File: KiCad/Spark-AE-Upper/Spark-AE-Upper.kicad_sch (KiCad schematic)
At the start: 15 parts, among them J1 SSM-120-L-SV-BE, J2 SSM-120-L-SV-BE, J4 Conn_02x05_Odd_Even, J5 Conn_01x08_Socket, J6 Conn_01x08_Socket, J7 UJ32-C-V-G-TH-5-P24-TR, SW1 SW_Push, SW2 SW_Push, U1 PJS008U-3000-0, U2 Daisy_Seed

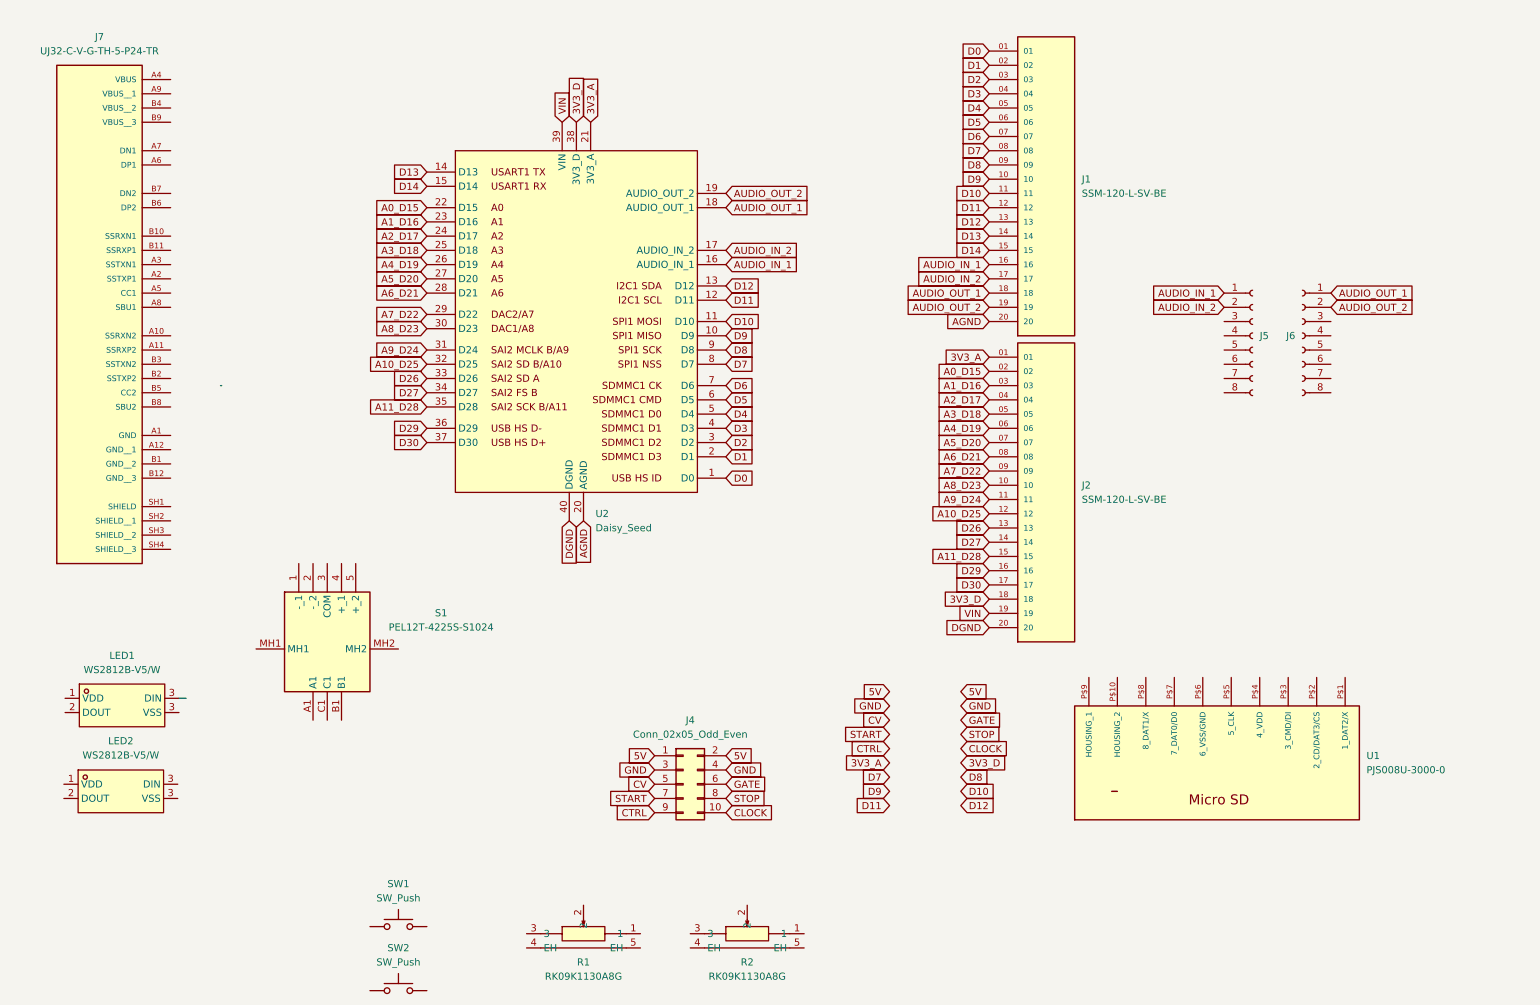
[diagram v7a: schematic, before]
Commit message: renamed nets to match pod and added arc connector
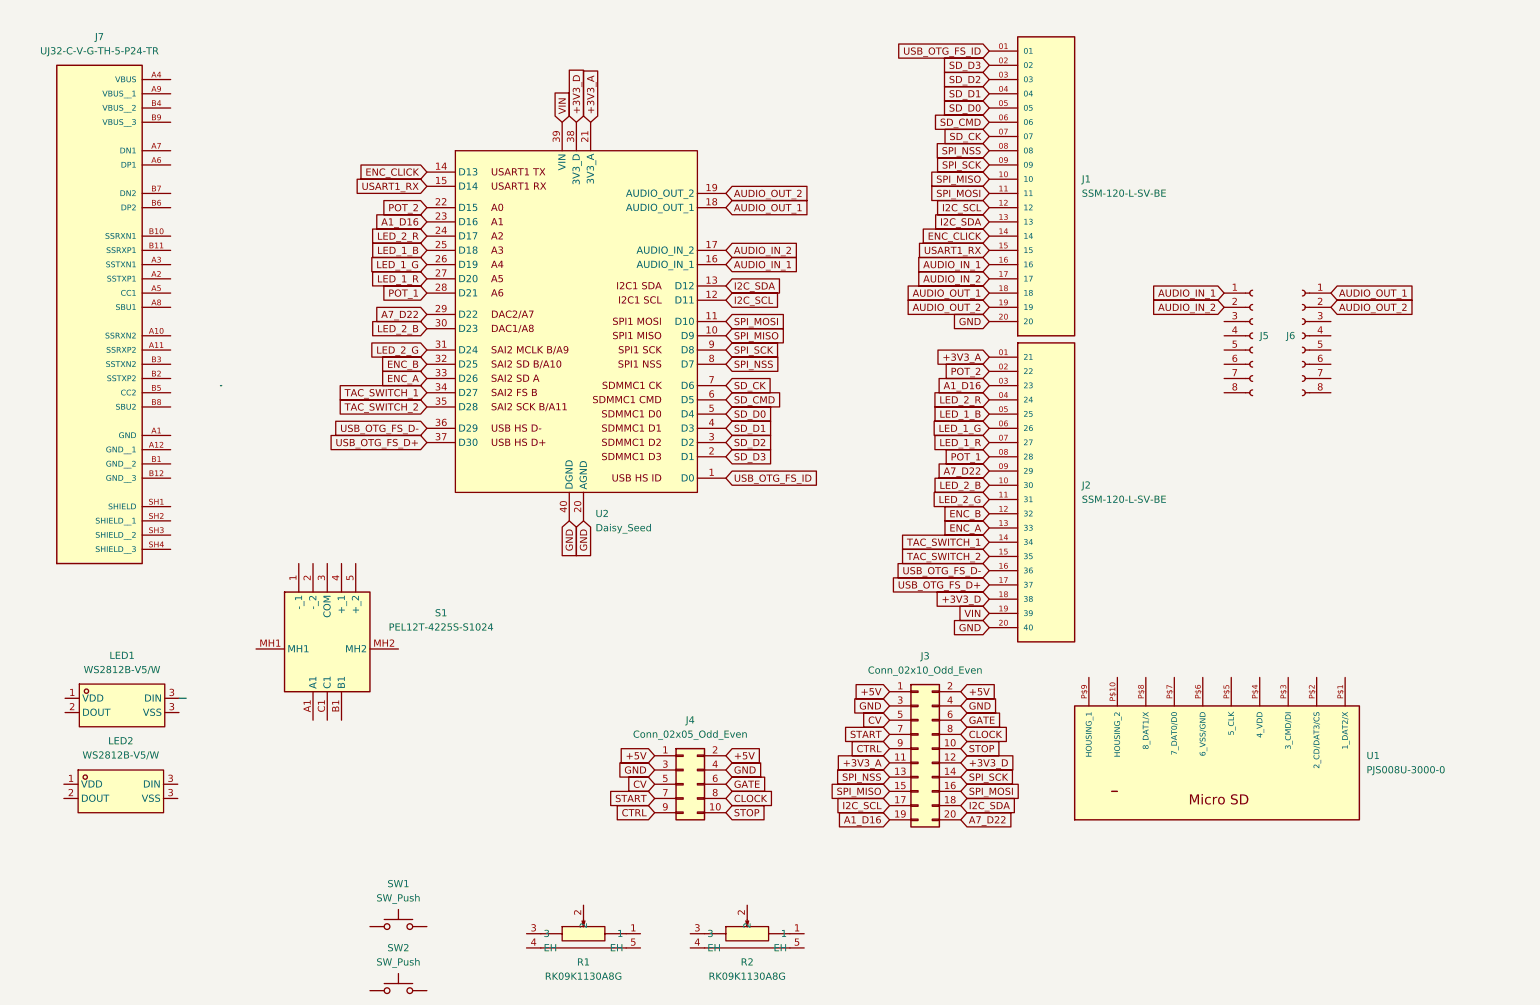
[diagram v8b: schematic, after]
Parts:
- added J3: Conn_02x10_Odd_Even, Connector_PinHeader_2.54mm:PinHeader_2x10_P2.54mm_Vertical, symbol Connector_Generic:Conn_02x10_Odd_Even
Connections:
- net AGND is gone; now on net GND: J1.20, U2.20 (AGND)
- net DGND is gone; now on net GND: J2.20 (40), U2.40 (DGND)
- net A1_D16: now also J3.19 (Pin_19)
- net A7_D22: now also J3.20 (Pin_20)
- net CLOCK: now also J4.8 (Pin_8), J3.8 (Pin_8); no longer J4.10 (Pin_10)
- net CTRL: now also J3.9 (Pin_9)
- net CV: now also J3.5 (Pin_5)
- net GATE: now also J3.6 (Pin_6)
- net GND: now also J3.3 (Pin_3), J3.4 (Pin_4)
- net START: now also J3.7 (Pin_7)
- net STOP: now also J4.10 (Pin_10), J3.10 (Pin_10); no longer J4.8 (Pin_8)
- net 3V3_A renamed +3V3_A
- net +3V3_A: now also J3.11 (Pin_11)
- net 3V3_D renamed +3V3_D
- net +3V3_D: now also J3.12 (Pin_12)
- net 5V renamed +5V
- net +5V: now also J3.1 (Pin_1), J3.2 (Pin_2)
- net A0_D15 renamed POT_2
- net A10_D25 renamed ENC_B
- net A11_D28 renamed TAC_SWITCH_2
- net A2_D17 renamed LED_2_R
- net A3_D18 renamed LED_1_B
- net A4_D19 renamed LED_1_G
- net A5_D20 renamed LED_1_R
- net A6_D21 renamed POT_1
- net A8_D23 renamed LED_2_B
- net A9_D24 renamed LED_2_G
- net D0 renamed USB_OTG_FS_ID
- net D1 renamed SD_D3
- net D10 renamed SPI_MOSI
- net SPI_MOSI: now also J3.16 (Pin_16)
- net D11 renamed I2C_SCL
- net I2C_SCL: now also J3.17 (Pin_17)
- net D12 renamed I2C_SDA
- net I2C_SDA: now also J3.18 (Pin_18)
- net D13 renamed ENC_CLICK
- net D14 renamed USART1_RX
- net D2 renamed SD_D2
- net D26 renamed ENC_A
- net D27 renamed TAC_SWITCH_1
- net D29 renamed USB_OTG_FS_D-
- net D3 renamed SD_D1
- net D30 renamed USB_OTG_FS_D+
- net D4 renamed SD_D0
- net D5 renamed SD_CMD
- net D6 renamed SD_CK
- net D7 renamed SPI_NSS
- net SPI_NSS: now also J3.13 (Pin_13)
- net D8 renamed SPI_SCK
- net SPI_SCK: now also J3.14 (Pin_14)
- net D9 renamed SPI_MISO
- net SPI_MISO: now also J3.15 (Pin_15)
